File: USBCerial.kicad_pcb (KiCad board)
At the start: 2 copper layers, 76.2 x 25.4 mm, 3 parts, among them J1 USB_C, U1 CH340C

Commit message: First schematic complete using the CH340C
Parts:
- added C2: 0.1uF 50V, Capacitor_SMD:C_0603_1608Metric_Pad1.08x0.95mm_HandSolder, F.Cu at (34.3, 35.3)
- added C3: 1uF 50V, Capacitor_SMD:C_0603_1608Metric_Pad1.08x0.95mm_HandSolder, F.Cu at (29.6, 44.5)
- added C4: 1uF 50V, Capacitor_SMD:C_0603_1608Metric_Pad1.08x0.95mm_HandSolder, F.Cu at (36.8, 29.8)
- added JP1: Jumper, Connector_PinHeader_2.54mm:PinHeader_1x03_P2.54mm_Vertical, F.Cu at (36.2, 45.1)
- added U2: XC6206P332MR, Package_TO_SOT_SMD:SOT-23, F.Cu at (33.7, 29.8)
- C1: value 0.1uF -> 0.1uF 50V; footprint Capacitor_SMD:C_0603_1608Metric -> Capacitor_SMD:C_0603_1608Metric_Pad1.08x0.95mm_HandSolder
- moved U1 8.32 mm to (39.4, 37.5)
- moved C1 6.00 mm to (29.6, 30.5), turned to 0 degrees
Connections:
- net GND renamed GNDD
- net Net-(U1-Pad13) renamed /DTR
- net Net-(U1-Pad14) renamed /RTS
- net Net-(U1-Pad2) renamed /TXD
- net Net-(U1-Pad3) renamed /RXD
- net Net-(U1-Pad9) renamed /CTS
- J1 pad A6: USB_D- -> /USB_D+
- J1 pad A7: USB_D+ -> /USB_D-
- J1 pad B6: USB_D- -> /USB_D+
- J1 pad B7: USB_D+ -> /USB_D-
- U1 pad 16: Net-(U1-Pad16) -> VCC
- U1 pad 4: Net-(U1-Pad4) -> +3V3
- U1 pad 5: Net-(U1-Pad5) -> /USB_D+
- U1 pad 6: Net-(U1-Pad6) -> /USB_D-
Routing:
- net +5V: track 0.00 -> 28.0 mm
- net +3V3: track 0.00 -> 23.1 mm
- net VCC: track 0.00 -> 14.1 mm, vias 0 -> 1
- net /USB_D-: track 0.00 -> 7.69 mm
- net /USB_D+: track 0.00 -> 7.45 mm
- net GNDD: track 0.00 -> 2.70 mm
- net USB_D-: track 1.70 -> 0.00 mm
- net USB_D+: track 1.70 -> 0.00 mm

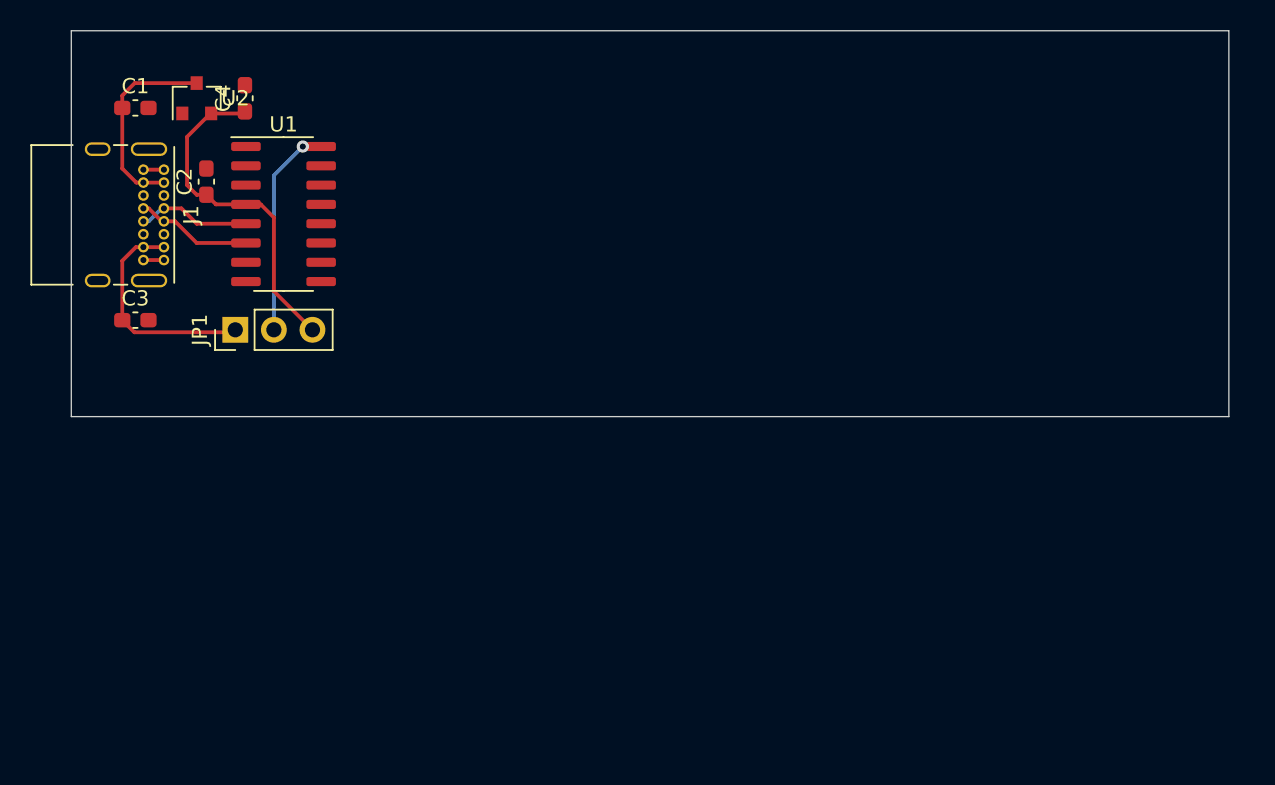
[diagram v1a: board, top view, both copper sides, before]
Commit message: Complete schematic, Begin on PCB placment and design
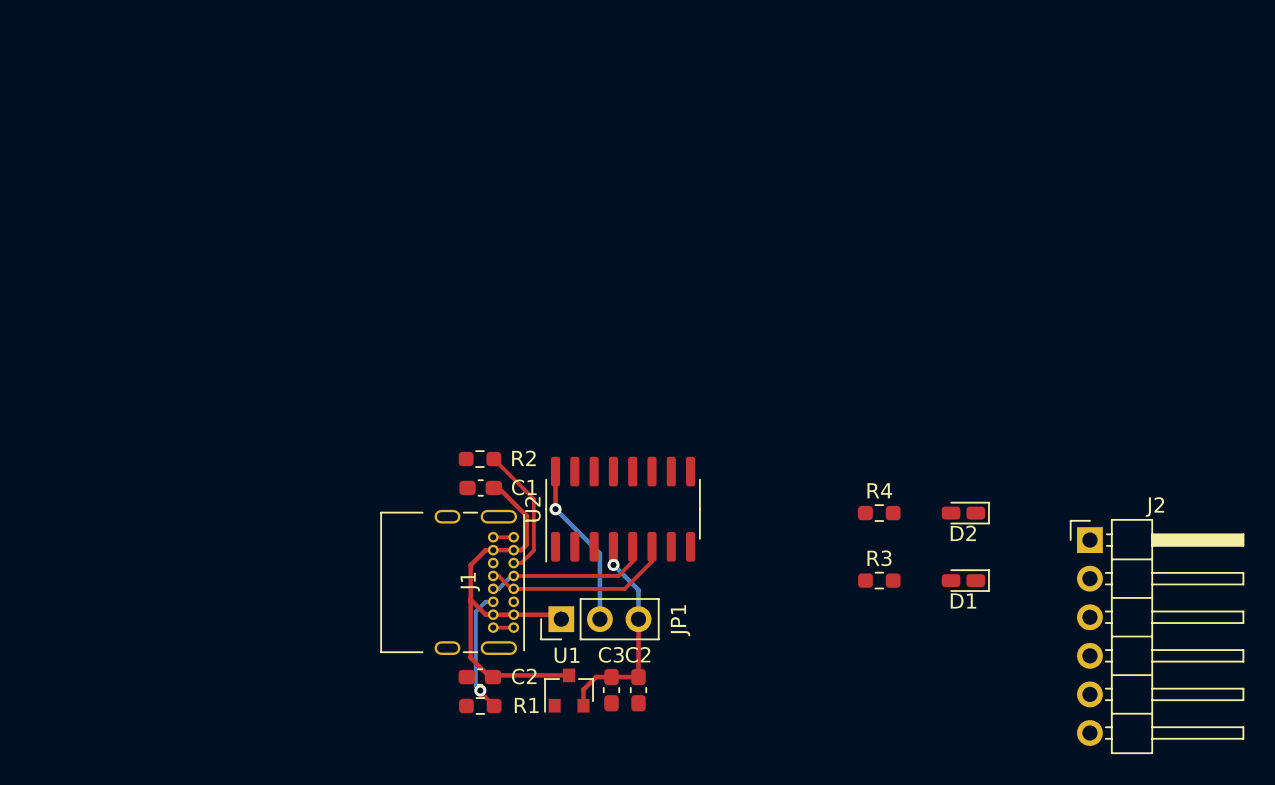
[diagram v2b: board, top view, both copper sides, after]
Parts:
- removed the C3 at (29.6, 44.5)
- added C2: 1uF 50V, Capacitor_SMD:C_0603_1608Metric_Pad1.08x0.95mm_HandSolder, F.Cu at (52.3, 67.9)
- added D1: LED_Small, LED_SMD:LED_0603_1608Metric_Castellated, F.Cu at (84.1, 61.6)
- added D2: LED_Small, LED_SMD:LED_0603_1608Metric_Castellated, F.Cu at (84.1, 57.1)
- added J2: Conn_01x06, Connector_PinHeader_2.54mm:PinHeader_1x06_P2.54mm_Horizontal, F.Cu at (92.5, 58.9)
- added R1: 5.1k, Resistor_SMD:R_0603_1608Metric_Pad0.98x0.95mm_HandSolder, F.Cu at (52.3, 69.8)
- added R2: 5.1k, Resistor_SMD:R_0603_1608Metric_Pad0.98x0.95mm_HandSolder, F.Cu at (52.3, 53.6)
- added R3: 51, Resistor_SMD:R_0603_1608Metric_Pad0.98x0.95mm_HandSolder, F.Cu at (78.6, 61.6)
- added R4: 51, Resistor_SMD:R_0603_1608Metric_Pad0.98x0.95mm_HandSolder, F.Cu at (78.6, 57.1)
- C1, C2: value 0.1uF 50V -> 0.1uF
- C3: renamed from C4; value 1uF 50V -> 1uF
- moved U1 46.1 mm to (58.2, 68.8)
- moved C3 45.8 mm to (61.0, 68.8), turned to 270 degrees
- moved C2 43.9 mm to (62.7, 68.8), turned to 270 degrees
- moved C1 33.8 mm to (52.4, 55.5), turned to 180 degrees
- moved J1 33.4 mm to (54.5, 58.7)
- moved U2 29.6 mm to (61.7, 56.9), turned to 90 degrees
- moved JP1 28.7 mm to (57.7, 64.1)
- renumbered U2 to U1, U1 to U2
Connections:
- net /RTS renamed Net-(U2-Pad14)
- J1 pad A5: Net-(J1-PadA5) -> /CC1
- J1 pad B5: Net-(J1-PadB5) -> /CC2
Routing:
- net +3V3: track 23.1 -> 14.3 mm, vias 0 -> 1
- net /CC1: track 0.00 -> 8.77 mm
- net /CC2: track 0.00 -> 8.13 mm, vias 0 -> 1
- net /USB_D-: track 7.69 -> 12.5 mm
- net /USB_D+: track 7.45 -> 10.9 mm
- net VCC: track 14.1 -> 10.9 mm
- net +5V: track 28.0 -> 29.0 mm
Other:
- board outline removed
- net class VCC added: clearance 0.2, trace_width 0.3, via_dia 0.8, via_drill 0.4
